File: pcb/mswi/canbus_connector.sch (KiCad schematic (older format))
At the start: 1 part, among them J601 RJ45

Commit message: Schematics Annotated
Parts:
- renumbered J601 to J501
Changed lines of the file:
@@
 CAN_H
 $Comp
-L Connector:RJ45_Shielded J601
+L Connector:RJ45_Shielded J501
 U 1 1 5BE6C2F7
 P 5950 3400
-AR Path="/5AAD16DD/5BE6C2F7" Ref="J601"  Part="1"
+AR Path="/5AAD16DD/5BE6C2F7" Ref="J501"  Part="1"
 AR Path="/5DDDDD74/5BE6C2F7" Ref="J?"  Part="1"
-F 0 "J?" H 6150 3950 50  0000 C CNN
+F 0 "J501" H 6150 3950 50  0000 C CNN
 F 1 "RJ45" H 5800 3950 50  0000 C CNN
 F 2 "KicadZeniteSolarLibrary18:RJ45_YH59_01" H 5950 3400 50  0001 C CNN

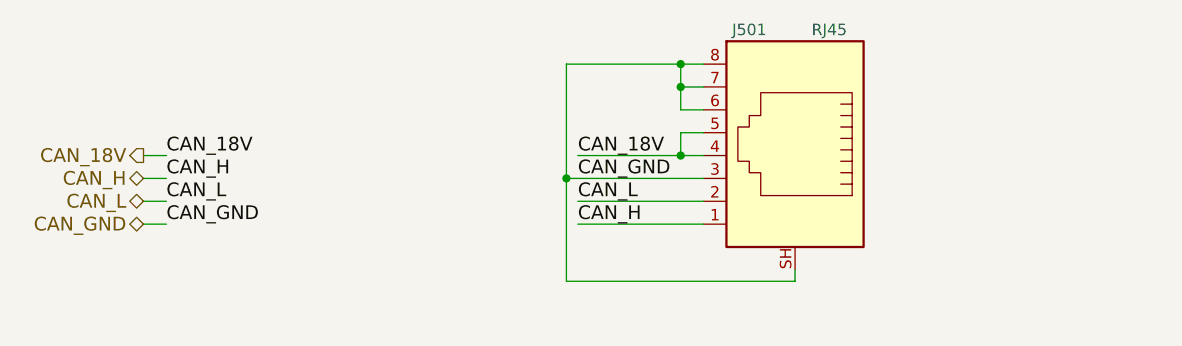
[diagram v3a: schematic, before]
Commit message: CANBUS connector changed
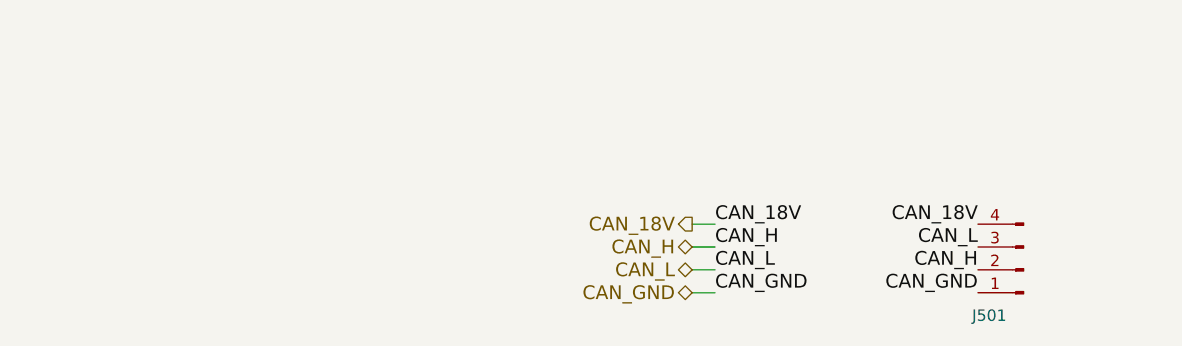
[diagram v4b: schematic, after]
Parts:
- removed J501: RJ45, KicadZeniteSolarLibrary18:RJ45_YH59_01, symbol Connector:RJ45_Shielded
- added J501: Conn_01x04_Male, symbol Connector:Conn_01x04_Male
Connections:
- net CAN_18V: now also J501.4 (Pin_4)
- net CAN_GND: now also J501.1 (Pin_1)
- net CAN_H: now also J501.2 (Pin_2)
- net CAN_L: now also J501.3 (Pin_3)
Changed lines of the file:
@@
 Comment4 ""
 $EndDescr
-Text HLabel 3100 3500 0    60   BiDi ~ 0
+Text HLabel 5500 3800 0    60   BiDi ~ 0
 CAN_H
-Text HLabel 3100 3600 0    60   BiDi ~ 0
+Text HLabel 5500 3900 0    60   BiDi ~ 0
 CAN_L
-Text HLabel 3100 3400 0    60   Output ~ 0
+Text HLabel 5500 3700 0    60   Output ~ 0
 CAN_18V
-Text HLabel 3100 3700 0    60   BiDi ~ 0
+Text HLabel 5500 4000 0    60   BiDi ~ 0
 CAN_GND
-Wire Wire Line
-	5950 3950 5950 3900
-Wire Wire Line
-	5000 3600 5550 3600
-Wire Wire Line
-	5550 3700 5000 3700
-Wire Wire Line
-	5000 3400 5450 3400
-Text Label 5000 3400 0    60   ~ 0
-CAN_18V
-Text Label 5000 3500 0    60   ~ 0
-CAN_GND
-Text Label 5000 3600 0    60   ~ 0
-CAN_L
-Text Label 5000 3700 0    60   ~ 0
-CAN_H
-$Comp
-L Connector:RJ45_Shielded J501
-U 1 1 5BE6C2F7
-P 5950 3400
-AR Path="/5AAD16DD/5BE6C2F7" Ref="J501"  Part="1"
-AR Path="/5DDDDD74/5BE6C2F7" Ref="J?"  Part="1"
-F 0 "J501" H 6150 3950 50  0000 C CNN
-F 1 "RJ45" H 5800 3950 50  0000 C CNN
-F 2 "KicadZeniteSolarLibrary18:RJ45_YH59_01" H 5950 3400 50  0001 C CNN
-F 3 "" H 5950 3400 50  0001 C CNN
-	1    5950 3400
-	-1   0    0    -1
-$EndComp
-Wire Wire Line
-	5550 3000 5450 3000
-Wire Wire Line
-	4950 3000 4950 3500
-Wire Wire Line
-	4950 3950 5950 3950
-Wire Wire Line
-	5550 3100 5450 3100
-Wire Wire Line
-	5450 3100 5450 3000
-Connection ~ 5450 3000
-Wire Wire Line
-	5450 3000 4950 3000
-Wire Wire Line
-	5550 3200 5450 3200
-Wire Wire Line
-	5550 3300 5450 3300
-Wire Wire Line
-	5450 3300 5450 3400
-Connection ~ 5450 3400
-Wire Wire Line
-	5450 3400 5550 3400
-Wire Wire Line
-	4950 3500 5550 3500
-Connection ~ 4950 3500
-Wire Wire Line
-	4950 3500 4950 3950
-Text Label 3200 3400 0    60   ~ 0
+Text Label 5600 3700 0    60   ~ 0
 CAN_18V
 Wire Wire Line
-	3100 3400 3200 3400
-Text Label 3200 3600 0    60   ~ 0
+	5500 3700 5600 3700
+Text Label 5600 3900 0    60   ~ 0
 CAN_L
-Text Label 3200 3500 0    60   ~ 0
+Text Label 5600 3800 0    60   ~ 0
 CAN_H
 Wire Wire Line
-	3100 3500 3200 3500
+	5500 3800 5600 3800
 Wire Wire Line
-	3200 3600 3100 3600
+	5600 3900 5500 3900
 Wire Wire Line
-	3100 3700 3200 3700
-Wire Wire Line
-	5450 3200 5450 3100
-Connection ~ 5450 3100
-Text Label 3200 3700 0    60   ~ 0
+	5500 4000 5600 4000
+Text Label 5600 4000 0    60   ~ 0
 CAN_GND
+$Comp
+L Connector:Conn_01x04_Male J501
+U 1 1 5DD7554D
+P 6950 3900
+F 0 "J501" H 7100 4100 50  0000 C CNN
+F 1 "Conn_01x04_Male" H 7100 4100 50  0001 C CNN
+F 2 "" H 6950 3900 50  0001 C CNN
+F 3 "~" H 6950 3900 50  0001 C CNN
+	1    6950 3900
+	-1   0    0    1
+$EndComp
+Text Label 6750 3700 2    60   ~ 0
+CAN_18V
+Text Label 6750 4000 2    60   ~ 0
+CAN_GND
+Text Label 6750 3800 2    60   ~ 0
+CAN_L
+Text Label 6750 3900 2    60   ~ 0
+CAN_H
 $EndSCHEMATC

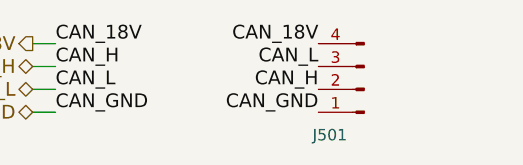
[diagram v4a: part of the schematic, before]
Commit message: CANBUS connector changed, footprint added
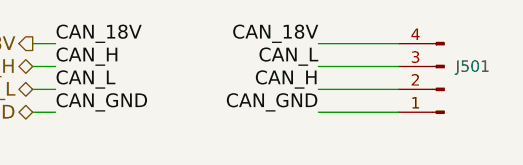
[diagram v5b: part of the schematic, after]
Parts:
- J501: footprint (none) -> Connector_PinHeader_2.54mm:PinHeader_1x04_P2.54mm_Horizontal
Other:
- moved on the sheet: J501
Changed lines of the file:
@@
 L Connector:Conn_01x04_Male J501
 U 1 1 5DD7554D
-P 6950 3900
-F 0 "J501" H 7100 4100 50  0000 C CNN
-F 1 "Conn_01x04_Male" H 7100 4100 50  0001 C CNN
-F 2 "" H 6950 3900 50  0001 C CNN
-F 3 "~" H 6950 3900 50  0001 C CNN
-	1    6950 3900
+P 7300 3900
+F 0 "J501" H 7250 3800 50  0000 R CNN
+F 1 "Conn_01x04_Male" H 7450 4100 50  0001 C CNN
+F 2 "Connector_PinHeader_2.54mm:PinHeader_1x04_P2.54mm_Horizontal" H 7300 3900 50  0001 C CNN
+F 3 "~" H 7300 3900 50  0001 C CNN
+	1    7300 3900
 	-1   0    0    1
 $EndComp
@@
 Text Label 6750 3900 2    60   ~ 0
 CAN_H
+Wire Wire Line
+	6750 3700 7100 3700
+Wire Wire Line
+	6750 3800 7100 3800
+Wire Wire Line
+	6750 3900 7100 3900
+Wire Wire Line
+	6750 4000 7100 4000
 $EndSCHEMATC
